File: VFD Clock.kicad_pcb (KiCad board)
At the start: 2 copper layers, 224 x 78 mm, 41 parts, among them J2 Mode Button, J3 Up Button, J4 Down Button, J5 Select Button, U1 74HC595, U10 74HC595, U11 UDN2981A, U12 Minute Right, U13 74HC595, U14 UDN2981A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

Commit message: adding hoppefully working one
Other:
- board text added: "I hope this works :)"
- board text added: "IV-11 VFD Tube Clock R.1 Made in Wisconsin Aron Szucs 2026"
- board text removed: "IV-11 VFD Tube Clock Made in Wisconsin Aron Szucs 2026"
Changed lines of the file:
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@@
 		(layer "Edge.Cuts")
 	)
-	(gr_text "IV-11 VFD Tube Clock\nMade in Wisconsin\nAron Szucs 2026\n"
+	(gr_text "IV-11 VFD Tube Clock R.1\nMade in Wisconsin\nAron Szucs 2026\n"
 		(at 272 80.5 270)
 		(layer "F.SilkS")
@@
 		)
 	)
+	(gr_text "I hope this works :)"
+		(at 282.5 142 270)
+		(layer "B.SilkS")
+		(effects
+			(font
+				(size 2 2)
+				(thickness 0.2)
+			)
+			(justify left bottom mirror)
+		)
+	)

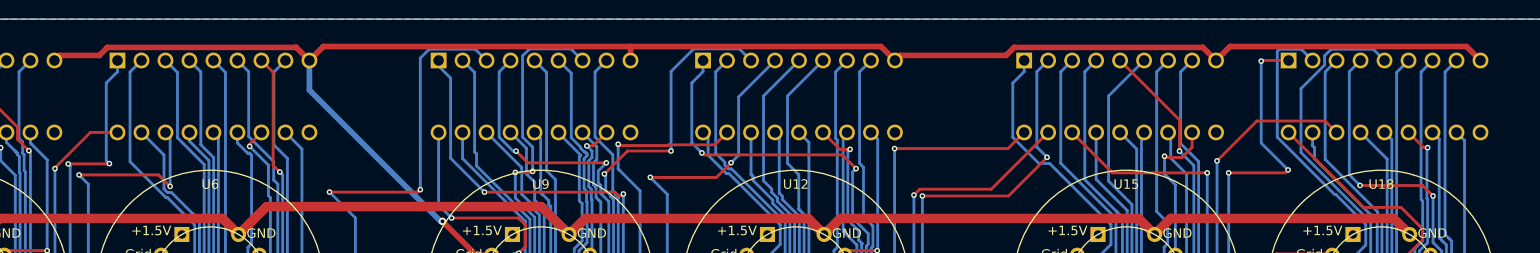
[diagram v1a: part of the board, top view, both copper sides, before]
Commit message: DFM check tweaks
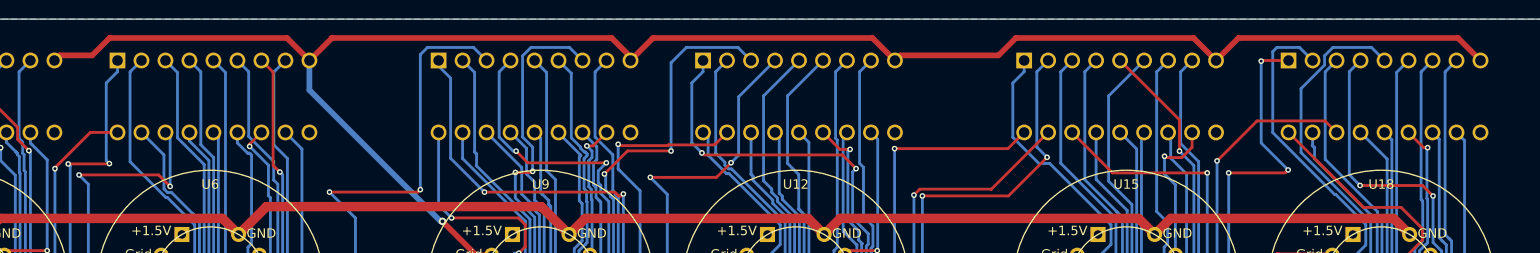
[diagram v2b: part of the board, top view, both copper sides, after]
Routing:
- net +25V: track 391.1 -> 394.9 mm
- net Net-(U16-QB): track 51.7 -> 52.6 mm
- net Net-(U10-QC): track 67.7 -> 68.3 mm

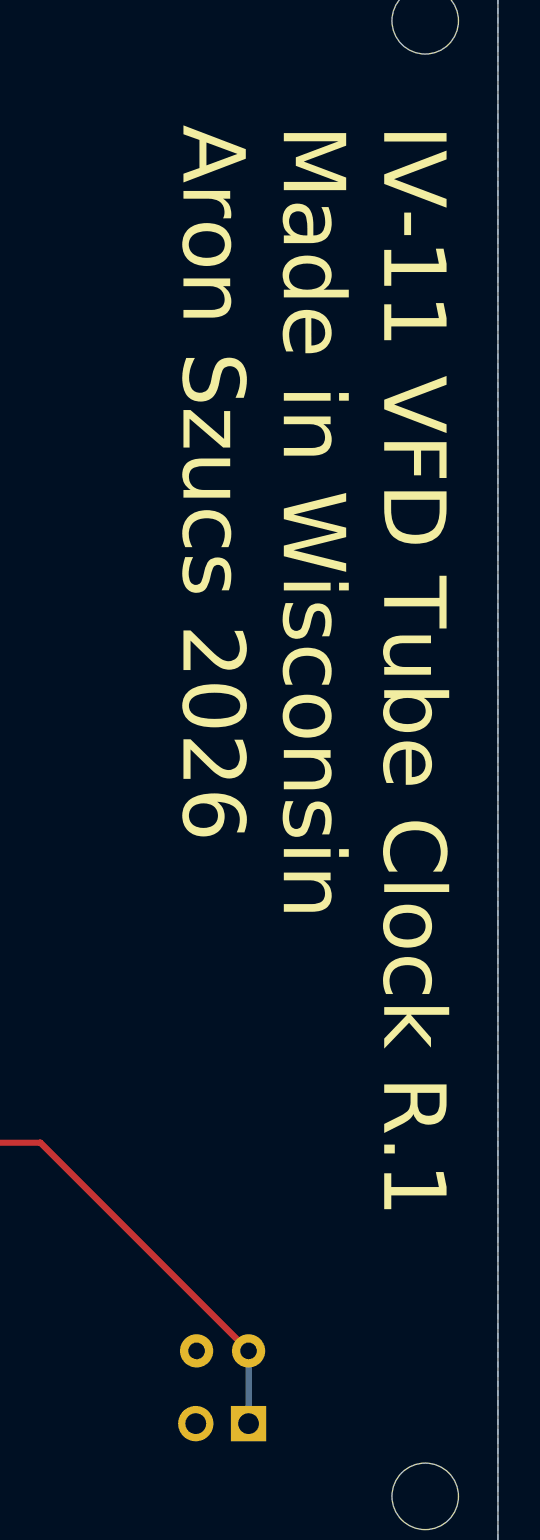
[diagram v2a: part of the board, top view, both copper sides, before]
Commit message: fixed tube code for PCB clock
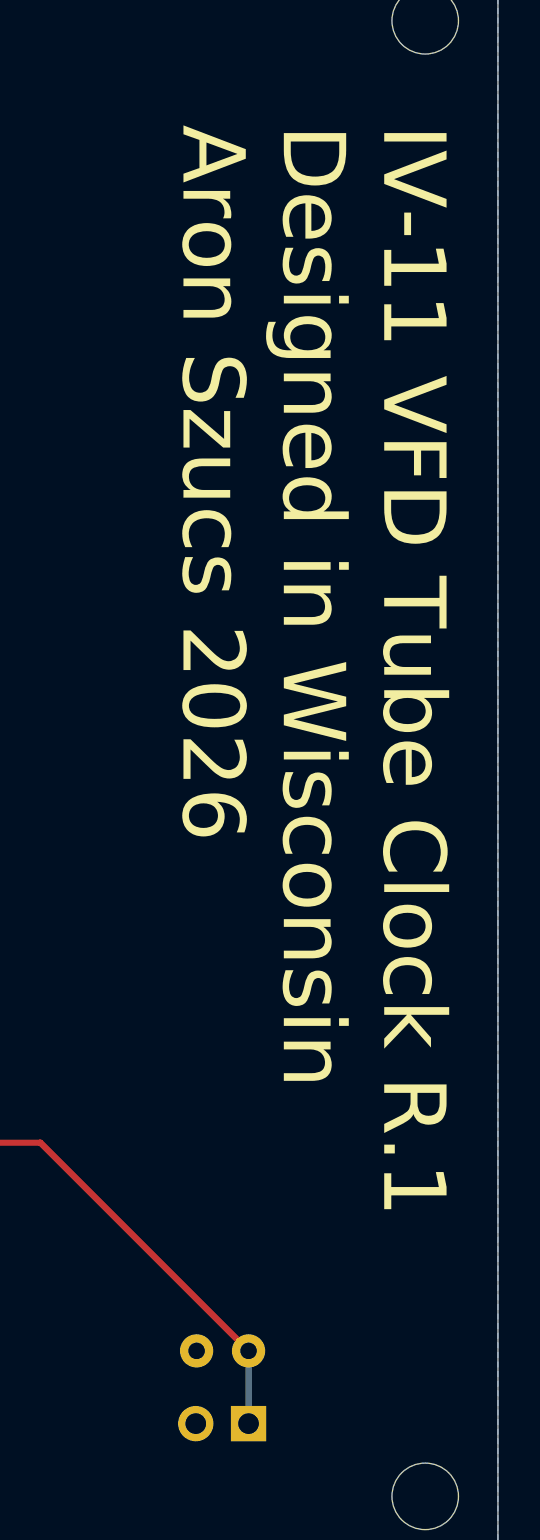
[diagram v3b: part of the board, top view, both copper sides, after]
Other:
- board text added: "IV-11 VFD Tube Clock R.1 Designed in Wisconsin Aron Szucs 2026"
- board text removed: "IV-11 VFD Tube Clock R.1 Made in Wisconsin Aron Szucs 2026"
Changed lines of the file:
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@@
 		(layer "Edge.Cuts")
 	)
-	(gr_text "IV-11 VFD Tube Clock R.1\nMade in Wisconsin\nAron Szucs 2026\n"
+	(gr_text "IV-11 VFD Tube Clock R.1\nDesigned in Wisconsin\nAron Szucs 2026\n"
 		(at 272 80.5 270)
 		(layer "F.SilkS")
